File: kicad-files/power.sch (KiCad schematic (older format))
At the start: 38 parts

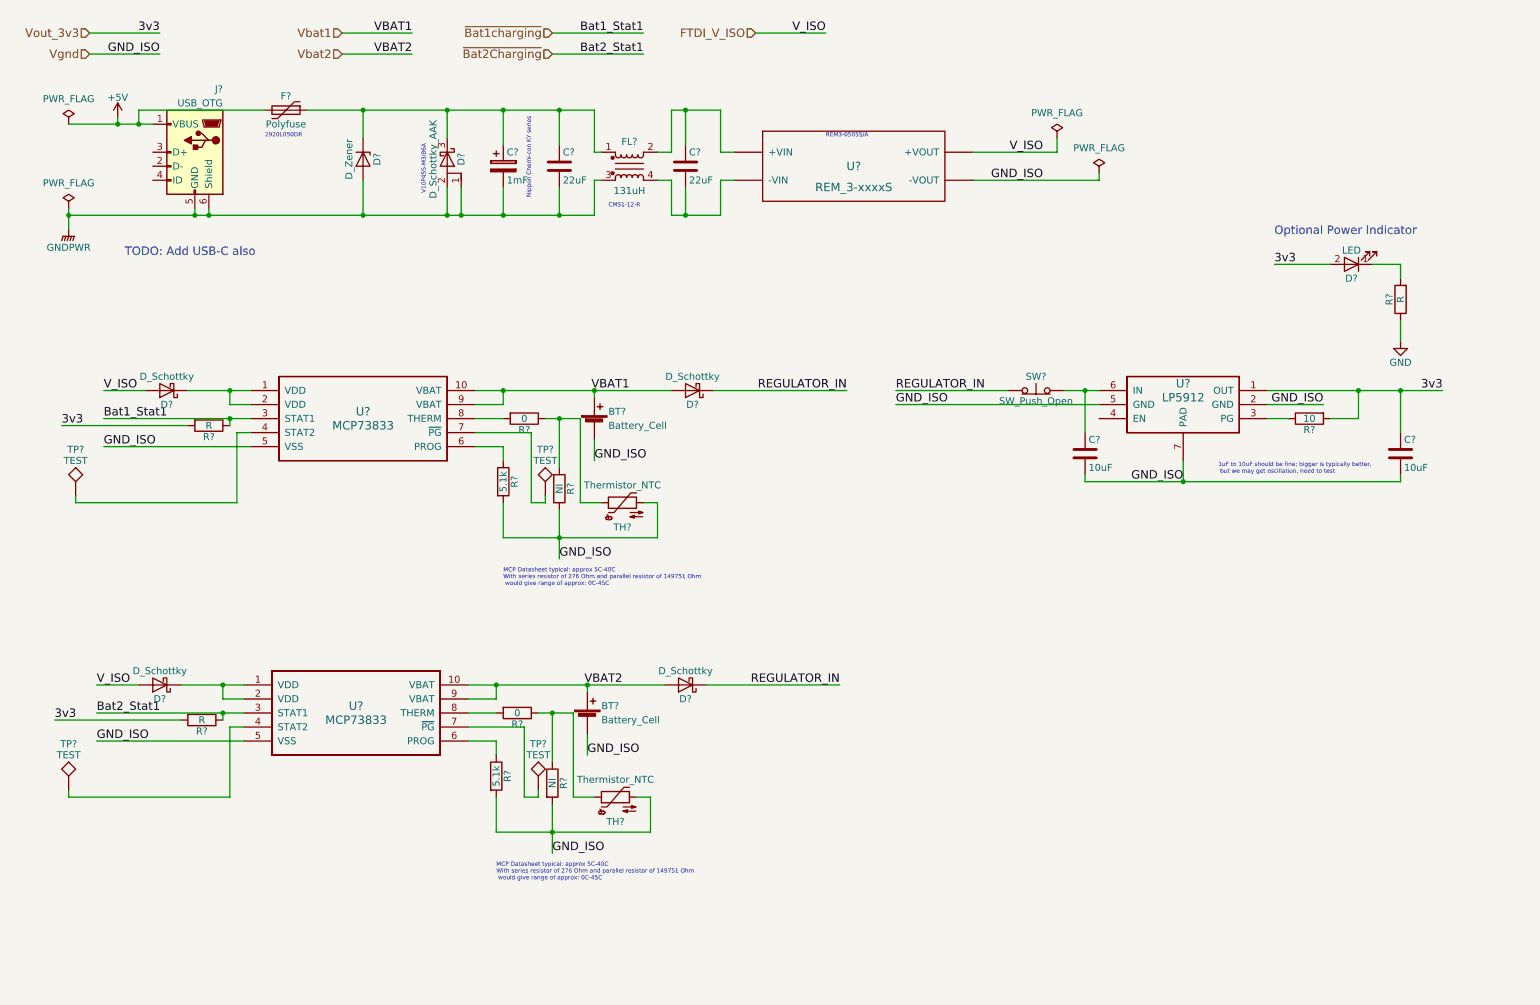
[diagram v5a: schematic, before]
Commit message: sketch-in USB C power option, TODO: add power muxer
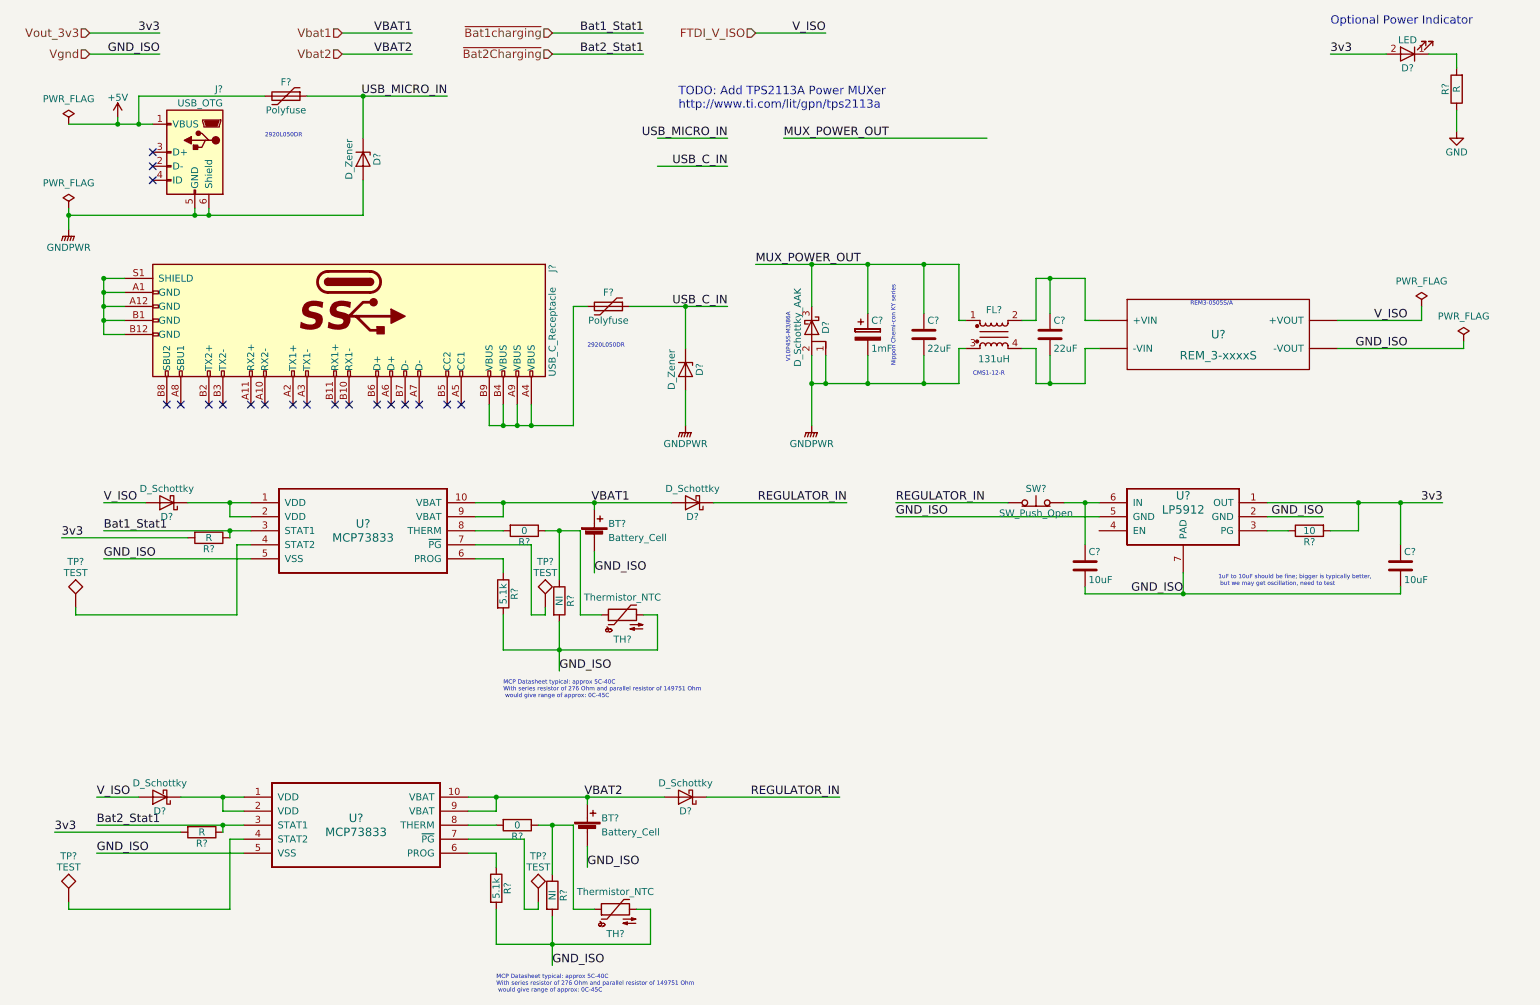
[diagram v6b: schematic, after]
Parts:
- added D?: D_Zener, symbol D_Zener
- added F?: Polyfuse, symbol Polyfuse
- added J?: USB_C_Receptacle, symbol USB_C_Receptacle
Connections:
- net GNDPWR: now also D?.2 (A)
- net MUX_POWER_OUT: now reaches C?.1, C?.1, D?.3 (K), FL?.1
- net MUX_POWER_OUT: no longer D?.1 (K), F?.1
- new net: J?.A1 (GND), J?.A12 (GND), J?.B1 (GND), J?.B12 (GND), J?.S1 (SHIELD)
- new net: F?.2, J?.A4 (VBUS), J?.A9 (VBUS), J?.B4 (VBUS), J?.B9 (VBUS)
- new net USB_C_IN: D?.1 (K), F?.1
- new net USB_MICRO_IN: D?.1 (K), F?.1
- no-connect marks 0 -> 19
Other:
- note added: "TODO: Add TPS2113A Power MUXer\nhttp://www.ti.com/lit/gpn/tps2113a"
- note removed: "TODO: Add USB-C also"
- moved on the sheet: BT?, C?, D?, F?, FL?, R?, SW?, TH?, TP?, U?

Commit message: multiplex power-in
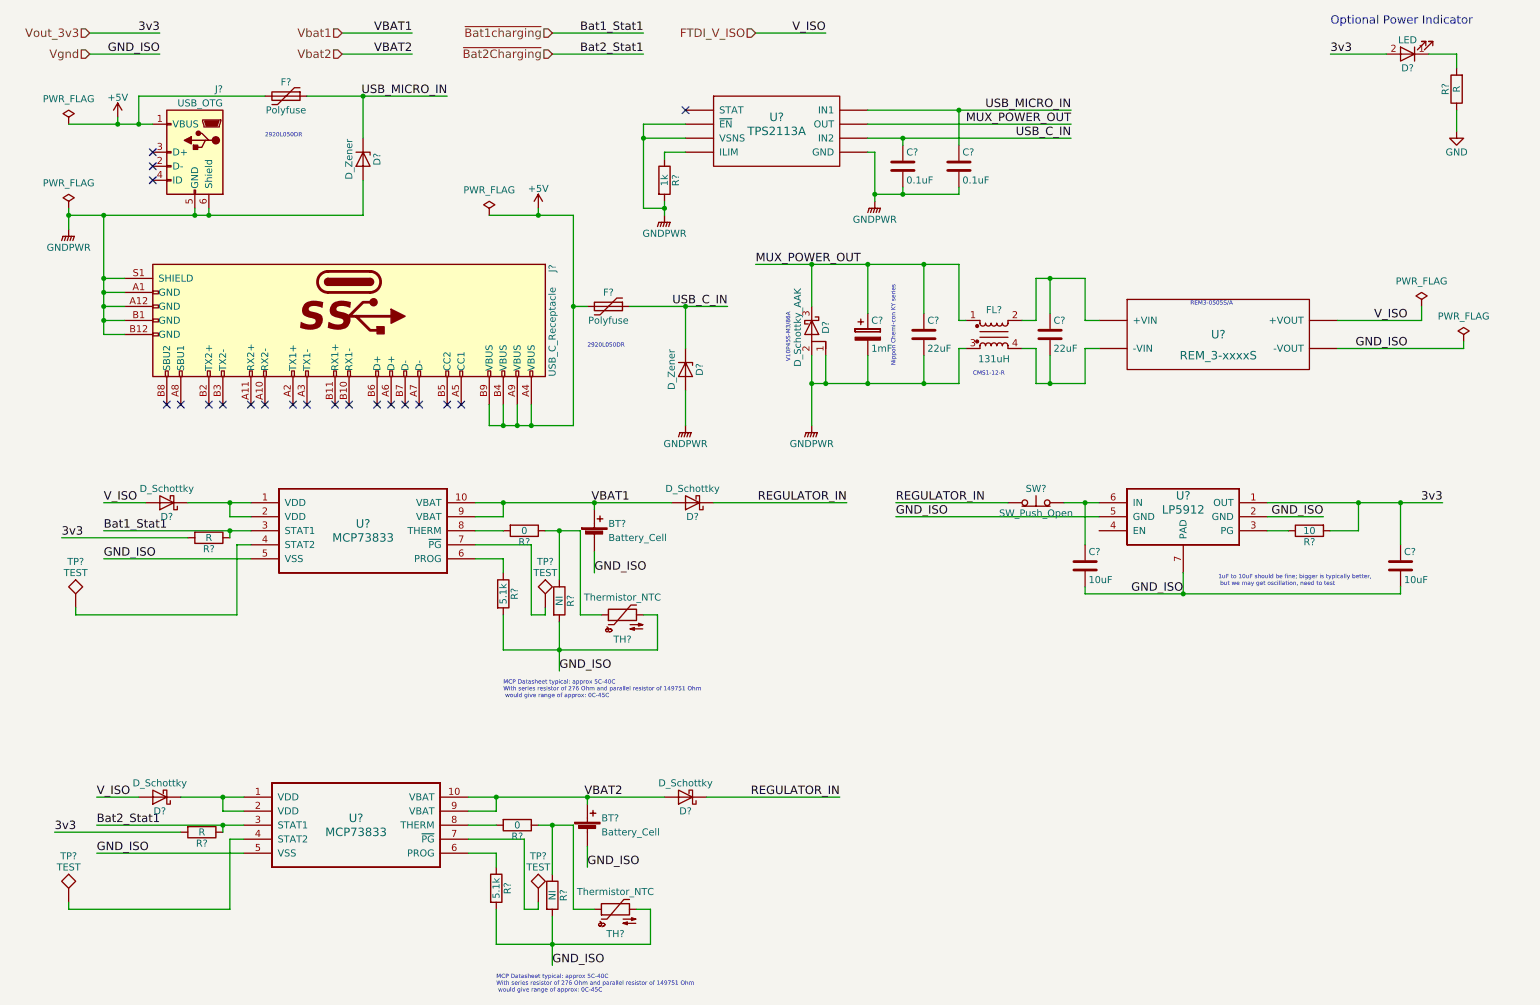
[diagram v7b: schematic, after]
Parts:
- added C? (x2): 0.1uF, symbol C
- added R?: 1k, symbol R
- added U?: TPS2113A, symbol TPS2113A
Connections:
- net +5V: now also F?.2, J?.A4 (VBUS), J?.A9 (VBUS), J?.B4 (VBUS), J?.B9 (VBUS)
- net GNDPWR: now also J?.A1 (GND), J?.A12 (GND), J?.B1 (GND), J?.B12 (GND), J?.S1 (SHIELD), C?.2, C?.2, R?.2, U?.~ (~EN~)
- net MUX_POWER_OUT: now also U?.~ (~EN~)
- net USB_C_IN: now also C?.1, U?.~ (~EN~)
- net USB_MICRO_IN: now also C?.1, U?.~ (~EN~)
- new net: R?.1, U?.~ (~EN~)
- no-connect marks 19 -> 20
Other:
- note removed: "TODO: Add TPS2113A Power MUXer\nhttp://www.ti.com/lit/gpn/tps2113a"
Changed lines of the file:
@@
 LIBS:rem_3-xxxxs
 LIBS:switches
+LIBS:tps2113a
 LIBS:OpenHardwareHolterMonitor-cache
 EELAYER 25 0
@@
 	5000 4800 5100 4800
 Wire Wire Line
-	5100 4800 5100 5050
-Wire Wire Line
-	5100 5050 4000 5050
+	5100 5050 5100 4800
+Wire Wire Line
+	4000 5050 5100 5050
 Connection ~ 4400 5050
 Wire Wire Line
@@
 	4950 6900 5050 6900
 Wire Wire Line
-	5050 6900 5050 7150
-Wire Wire Line
-	5050 7150 3950 7150
+	5050 7150 5050 6900
+Wire Wire Line
+	3950 7150 5050 7150
 Connection ~ 4350 7150
 Wire Wire Line
@@
 Connection ~ 1800 1950
 Wire Wire Line
-	1150 2400 1150 2800
+	1150 1950 1150 2800
 Wire Wire Line
 	1150 2800 1300 2800
@@
 Connection ~ 1150 2400
 Wire Wire Line
-	3900 3450 4500 3450
+	4500 3450 3900 3450
 Wire Wire Line
 	4200 3450 4200 3300
@@
 Connection ~ 4000 3450
 Wire Wire Line
-	3900 3300 3900 3450
+	3900 3450 3900 3300
 Wire Wire Line
 	1400 1100 2300 1100
@@
 	5300 3200 5300 3450
 Wire Wire Line
-	4500 3450 4500 2600
+	4500 1950 4500 3450
 Wire Wire Line
 	4500 2600 4600 2600
@@
 Text Label 5800 2300 0    60   ~ 0
 MUX_POWER_OUT
-Text Notes 5250 1200 0    60   ~ 0
-TODO: Add TPS2113A Power MUXer\nhttp://www.ti.com/lit/gpn/tps2113a
-Wire Wire Line
-	5600 1400 5100 1400
-Wire Wire Line
-	5600 1600 5100 1600
-Text Label 5600 1400 2    60   ~ 0
+Wire Wire Line
+	6600 1200 8050 1200
+Text Label 8050 1200 2    60   ~ 0
 USB_MICRO_IN
-Text Label 5600 1600 2    60   ~ 0
+Text Label 8050 1400 2    60   ~ 0
 USB_C_IN
 Wire Wire Line
-	6000 1400 7450 1400
-Text Label 6000 1400 0    60   ~ 0
+	6600 1300 8050 1300
+Text Label 8050 1300 2    60   ~ 0
 MUX_POWER_OUT
+Connection ~ 1150 1950
+$Comp
+L +5V #PWR?
+U 1 1 5B0B5DC1
+P 4250 1900
+F 0 "#PWR?" H 4250 1750 50  0001 C CNN
+F 1 "+5V" H 4250 2040 50  0000 C CNN
+F 2 "" H 4250 1900 50  0000 C CNN
+F 3 "" H 4250 1900 50  0000 C CNN
+	1    4250 1900
+	1    0    0    -1
+$EndComp
+$Comp
+L PWR_FLAG #FLG?
+U 1 1 5B0B5DC7
+P 3900 1950
+F 0 "#FLG?" H 3900 2045 50  0001 C CNN
+F 1 "PWR_FLAG" H 3900 2130 50  0000 C CNN
+F 2 "" H 3900 1950 50  0000 C CNN
+F 3 "" H 3900 1950 50  0000 C CNN
+	1    3900 1950
+	1    0    0    -1
+$EndComp
+Wire Wire Line
+	3900 1950 4500 1950
+Wire Wire Line
+	4250 1950 4250 1900
+Connection ~ 4250 1950
+Connection ~ 4500 2600
+$Comp
+L TPS2113A U?
+U 1 1 5B098D22
+P 5950 1350
+F 0 "U?" H 5950 1450 60  0000 C CNN
+F 1 "TPS2113A" H 5950 1350 60  0000 C CNN
+F 2 "" H 5950 1350 60  0001 C CNN
+F 3 "" H 5950 1350 60  0001 C CNN
+	1    5950 1350
+	1    0    0    -1
+$EndComp
+Wire Wire Line
+	6600 1500 6650 1500
+Wire Wire Line
+	6650 1500 6650 1850
+$Comp
+L GNDPWR #PWR?
+U 1 1 5B09AD74
+P 6650 1850
+F 0 "#PWR?" H 6650 1650 50  0001 C CNN
+F 1 "GNDPWR" H 6650 1720 50  0000 C CNN
+F 2 "" H 6650 1800 50  0001 C CNN
+F 3 "" H 6650 1800 50  0001 C CNN
+	1    6650 1850
+	1    0    0    -1
+$EndComp
+NoConn ~ 5300 1200
+$Comp
+L R R?
+U 1 1 5B0A89E4
+P 5150 1700
+F 0 "R?" V 5230 1700 50  0000 C CNN
+F 1 "1k" V 5150 1700 50  0000 C CNN
+F 2 "" V 5080 1700 50  0001 C CNN
+F 3 "" H 5150 1700 50  0001 C CNN
+	1    5150 1700
+	1    0    0    -1
+$EndComp
+Wire Wire Line
+	5300 1500 5150 1500
+Wire Wire Line
+	5150 1500 5150 1550
+Wire Wire Line
+	5150 1850 5150 1950
+$Comp
+L GNDPWR #PWR?
+U 1 1 5B0A8CC2
+P 5150 1950
+F 0 "#PWR?" H 5150 1750 50  0001 C CNN
+F 1 "GNDPWR" H 5150 1820 50  0000 C CNN
+F 2 "" H 5150 1900 50  0001 C CNN
+F 3 "" H 5150 1900 50  0001 C CNN
+	1    5150 1950
+	1    0    0    -1
+$EndComp
+Wire Wire Line
+	5300 1300 5000 1300
+Wire Wire Line
+	5000 1300 5000 1900
+Wire Wire Line
+	5000 1900 5150 1900
+Connection ~ 5150 1900
+Wire Wire Line
+	5300 1400 5000 1400
+Connection ~ 5000 1400
+$Comp
+L C C?
+U 1 1 5B0AAD39
+P 6850 1600
+F 0 "C?" H 6875 1700 50  0000 L CNN
+F 1 "0.1uF" H 6875 1500 50  0000 L CNN
+F 2 "" H 6888 1450 50  0001 C CNN
+F 3 "" H 6850 1600 50  0001 C CNN
+	1    6850 1600
+	1    0    0    -1
+$EndComp
+Wire Wire Line
+	7250 1200 7250 1450
+Connection ~ 7250 1200
+Wire Wire Line
+	7250 1800 7250 1750
+Connection ~ 6650 1800
+$Comp
+L C C?
+U 1 1 5B0C34BA
+P 7250 1600
+F 0 "C?" H 7275 1700 50  0000 L CNN
+F 1 "0.1uF" H 7275 1500 50  0000 L CNN
+F 2 "" H 7288 1450 50  0001 C CNN
+F 3 "" H 7250 1600 50  0001 C CNN
+	1    7250 1600
+	1    0    0    -1
+$EndComp
+Wire Wire Line
+	6600 1400 8050 1400
+Wire Wire Line
+	6850 1400 6850 1450
+Connection ~ 6850 1400
+Wire Wire Line
+	6850 1750 6850 1800
+Wire Wire Line
+	6650 1800 7250 1800
+Connection ~ 6850 1800
 $EndSCHEMATC

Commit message: fix rules-check issues
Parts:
- gave numbers to parts that had none: 45
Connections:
- net +5V: no longer F2.2, J3.A4 (VBUS), J3.A9 (VBUS), J3.B4 (VBUS), J3.B9 (VBUS)
- net REGULATOR_IN: now also U6.4 (EN)
- new net +5C: F2.2, J3.A4 (VBUS), J3.A9 (VBUS), J3.B4 (VBUS), J3.B9 (VBUS)
